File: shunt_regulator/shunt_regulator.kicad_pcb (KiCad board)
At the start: 2 copper layers, 87.5 x 94 mm, 58 parts, among them J1 Screw_Terminal_01x03, Q1 BC846B, Q2 BC846B, Q3 BC856B, Q4 30N06, U1 LM317_TO-252, U2 LM393

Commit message: Fixed a push-pull transistor that was the wrong way around
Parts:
- moved Q3 0.11 mm to (26.2, 18.5), turned to 90 degrees
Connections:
- Q3 pad 2: GND -> Net-(Q2-Pad2)
- Q3 pad 3: Net-(Q2-Pad2) -> GND
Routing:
- net Net-(Q3-Pad1): track 5.56 -> 7.08 mm
- net GND: track 84.0 -> 82.5 mm, vias 24 -> 25
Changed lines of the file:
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@@
   (net 6 "Net-(Q1-Pad1)")
   (net 7 "Net-(Q1-Pad2)")
-  (net 8 "Net-(Q2-Pad1)")
+  (net 8 "Net-(Q3-Pad1)")
   (net 9 "Net-(Q2-Pad2)")
   (net 10 "Net-(Q4-Pad1)")
@@
   )
   (footprint "Package_TO_SOT_SMD:SOT-23" (layer "F.Cu")
-    (at 26.162 18.431)
+    (at 26.162 18.542 90)
     (descr "SOT, 3 Pin (https://www.jedec.org/system/files/docs/to-236h.pdf variant AB), generated with kicad-footprint-generator ipc_gullwing_generator.py")
     (tags "SOT TO_SOT_SMD")
@@
     (property "Sheetname" "")
     (attr smd)
-    (fp_text reference "Q3" (at 3.838 1.069) (layer "F.SilkS")
-      (effects (font (size 1 1) (thickness 0.15)))
-    )
-    (fp_text value "BC856B" (at 0 2.4) (layer "F.Fab")
-      (effects (font (size 1 1) (thickness 0.15)))
-    )
-    (fp_text user "${REFERENCE}" (at 0 0) (layer "F.Fab")
+    (fp_text reference "Q3" (at 3.838 1.069 90) (layer "F.SilkS")
+      (effects (font (size 1 1) (thickness 0.15)))
+    )
+    (fp_text value "BC856B" (at 0 2.4 90) (layer "F.Fab")
+      (effects (font (size 1 1) (thickness 0.15)))
+    )
+    (fp_text user "${REFERENCE}" (at 0 0 90) (layer "F.Fab")
       (effects (font (size 0.32 0.32) (thickness 0.05)))
     )
@@
     (fp_line (start -0.65 -1.125) (end -0.325 -1.45) (layer "F.Fab") (width 0.1))
     (fp_line (start -0.65 1.45) (end -0.65 -1.125) (layer "F.Fab") (width 0.1))
-    (pad "1" smd roundrect (at -0.9375 -0.95) (size 1.475 0.6) (layers "F.Cu" "F.Paste" "F.Mask") (roundrect_rratio 0.25)
-      (net 8 "Net-(Q2-Pad1)") (pinfunction "B") (pintype "input"))
-    (pad "2" smd roundrect (at -0.9375 0.95) (size 1.475 0.6) (layers "F.Cu" "F.Paste" "F.Mask") (roundrect_rratio 0.25)
-      (net 2 "GND") (pinfunction "E") (pintype "passive"))
-    (pad "3" smd roundrect (at 0.9375 0) (size 1.475 0.6) (layers "F.Cu" "F.Paste" "F.Mask") (roundrect_rratio 0.25)
-      (net 9 "Net-(Q2-Pad2)") (pinfunction "C") (pintype "passive"))
+    (pad "1" smd roundrect (at -0.9375 -0.95 90) (size 1.475 0.6) (layers "F.Cu" "F.Paste" "F.Mask") (roundrect_rratio 0.25)
+      (net 8 "Net-(Q3-Pad1)") (pinfunction "B") (pintype "input"))
+    (pad "2" smd roundrect (at -0.9375 0.95 90) (size 1.475 0.6) (layers "F.Cu" "F.Paste" "F.Mask") (roundrect_rratio 0.25)
+      (net 9 "Net-(Q2-Pad2)") (pinfunction "E") (pintype "passive"))
+    (pad "3" smd roundrect (at 0.9375 0 90) (size 1.475 0.6) (layers "F.Cu" "F.Paste" "F.Mask") (roundrect_rratio 0.25)
+      (net 2 "GND") (pinfunction "C") (pintype "passive"))
     (model "${KICAD6_3DMODEL_DIR}/Package_TO_SOT_SMD.3dshapes/SOT-23.wrl"
       (offset (xyz 0 0 0))
@@
     (fp_line (start -0.65 -1.125) (end -0.325 -1.45) (layer "F.Fab") (width 0.1))
     (pad "1" smd roundrect (at -0.9375 -0.95 90) (size 1.475 0.6) (layers "F.Cu" "F.Paste" "F.Mask") (roundrect_rratio 0.25)
-      (net 8 "Net-(Q2-Pad1)") (pinfunction "B") (pintype "input"))
+      (net 8 "Net-(Q3-Pad1)") (pinfunction "B") (pintype "input"))
     (pad "2" smd roundrect (at -0.9375 0.95 90) (size 1.475 0.6) (layers "F.Cu" "F.Paste" "F.Mask") (roundrect_rratio 0.25)
       (net 9 "Net-(Q2-Pad2)") (pinfunction "E") (pintype "passive"))
@@
       (net 15 "Net-(R10-Pad1)") (pintype "passive"))
     (pad "2" smd roundrect (at 0.9125 0) (size 1.025 1.4) (layers "F.Cu" "F.Paste" "F.Mask") (roundrect_rratio 0.243902439)
-      (net 8 "Net-(Q2-Pad1)") (pintype "passive"))
+      (net 8 "Net-(Q3-Pad1)") (pintype "passive"))
     (model "${KICAD6_3DMODEL_DIR}/Resistor_SMD.3dshapes/R_0805_2012Metric.wrl"
       (offset (xyz 0 0 0))
@@
   (segment (start -21.474528 12.346528) (end -19.431 10.303) (width 1) (layer "B.Cu") (net 1))
   (segment (start 44.726 4.969) (end 44.218 4.461) (width 2) (layer "F.Cu") (net 2))
-  (segment (start 28.645 19.631) (end 28.702 19.574) (width 1) (layer "F.Cu") (net 2))
   (segment (start 46.99 4.461) (end 45.466 4.461) (width 2) (layer "F.Cu") (net 2))
-  (segment (start 25.2245 19.381) (end 25.4745 19.631) (width 1) (layer "F.Cu") (net 2))
   (segment (start 45.593 6.62) (end 46.47 6.62) (width 2) (layer "F.Cu") (net 2))
   (segment (start 48.768 8.652) (end 47.752 8.652) (width 2) (layer "F.Cu") (net 2))
@@
   (segment (start 48.768 8.62011) (end 48.768 8.652) (width 2) (layer "F.Cu") (net 2))
   (segment (start 43.978 8.652) (end 44.218 8.412) (width 2) (layer "F.Cu") (net 2))
+  (segment (start 25.2245 17.6045) (end 25.146 17.526) (width 1) (layer "F.Cu") (net 2))
   (segment (start 23.005 11.591) (end 22.987 11.573) (width 1) (layer "F.Cu") (net 2))
   (segment (start 46.228 8.652) (end 44.704 8.652) (width 2) (layer "F.Cu") (net 2))
+  (segment (start 27.0995 17.6045) (end 27.178 17.526) (width 1) (layer "F.Cu") (net 2))
   (segment (start -27.7105 18.558) (end -27.7105 20.0575) (width 1) (layer "F.Cu") (net 2))
+  (segment (start 26.162 17.6045) (end 27.0995 17.6045) (width 1) (layer "F.Cu") (net 2))
   (segment (start 41.656 8.652) (end 43.18 8.652) (width 2) (layer "F.Cu") (net 2))
   (segment (start 24.3355 11.591) (end 23.005 11.591) (width 1) (layer "F.Cu") (net 2))
@@
   (segment (start 3.1515 19.574) (end 2.447 19.574) (width 1) (layer "F.Cu") (net 2))
   (segment (start 2.447 19.574) (end 1.778 18.905) (width 1) (layer "F.Cu") (net 2))
-  (segment (start 27.051 19.631) (end 28.645 19.631) (width 1) (layer "F.Cu") (net 2))
   (segment (start 46.978 6.112) (end 46.978 5.846) (width 2) (layer "F.Cu") (net 2))
   (segment (start 47.752 8.652) (end 46.228 8.652) (width 2) (layer "F.Cu") (net 2))
@@
   (segment (start 46.978 6.83011) (end 48.768 8.62011) (width 2) (layer "F.Cu") (net 2))
   (segment (start 16.572 14.429) (end 16.51 14.367) (width 1) (layer "F.Cu") (net 2))
-  (segment (start 25.4745 19.631) (end 27.051 19.631) (width 1) (layer "F.Cu") (net 2))
   (segment (start 44.218 8.412) (end 44.218 6.62) (width 2) (layer "F.Cu") (net 2))
   (segment (start 2.9995 13.605) (end 1.143 13.605) (width 1) (layer "F.Cu") (net 2))
+  (segment (start 26.162 17.6045) (end 25.2245 17.6045) (width 1) (layer "F.Cu") (net 2))
   (segment (start 46.978 6.112) (end 46.978 6.83011) (width 2) (layer "F.Cu") (net 2))
   (segment (start 44.218 6.62) (end 45.593 6.62) (width 2) (layer "F.Cu") (net 2))
@@
   (via (at 1.778 18.905) (size 1) (drill 0.5) (layers "F.Cu" "B.Cu") (net 2))
   (via (at 41.656 8.652) (size 1) (drill 0.5) (layers "F.Cu" "B.Cu") (net 2))
-  (via (at 28.702 19.574) (size 1) (drill 0.5) (layers "F.Cu" "B.Cu") (net 2))
   (via (at 45.593 6.62) (size 1) (drill 0.5) (layers "F.Cu" "B.Cu") (net 2))
   (via (at 41.452 18) (size 1) (drill 0.5) (layers "F.Cu" "B.Cu") (net 2))
@@
   (via (at -27.686 20.082) (size 1) (drill 0.5) (layers "F.Cu" "B.Cu") (net 2))
   (via (at 44.5 18) (size 1) (drill 0.5) (layers "F.Cu" "B.Cu") (net 2))
+  (via (at 27.178 17.526) (size 1) (drill 0.5) (layers "F.Cu" "B.Cu") (net 2))
   (via (at 46.024 18) (size 1) (drill 0.5) (layers "F.Cu" "B.Cu") (net 2))
   (via (at 49.072 18) (size 1) (drill 0.5) (layers "F.Cu" "B.Cu") (net 2))
@@
   (via (at 42.976 18) (size 1) (drill 0.5) (layers "F.Cu" "B.Cu") (net 2))
   (via (at 45.466 4.461) (size 1) (drill 0.5) (layers "F.Cu" "B.Cu") (net 2))
+  (via (at 25.146 17.526) (size 1) (drill 0.5) (layers "F.Cu" "B.Cu") (net 2))
   (via (at 47.752 8.652) (size 1) (drill 0.5) (layers "F.Cu" "B.Cu") (net 2))
   (via (at 44.218 4.461) (size 1) (drill 0.5) (layers "F.Cu" "B.Cu") (net 2))
@@
   (segment (start 6.858 17.7725) (end 5.196 17.7725) (width 1) (layer "F.Cu") (net 7))
   (segment (start 4.9765 17.553) (end 4.887 17.4635) (width 1) (layer "F.Cu") (net 7))
-  (segment (start 22.78 19.193) (end 22.78 18.384) (width 1) (layer "F.Cu") (net 8))
-  (segment (start 23.683 17.481) (end 25.2245 17.481) (width 1) (layer "F.Cu") (net 8))
-  (segment (start 22.78 18.384) (end 23.683 17.481) (width 1) (layer "F.Cu") (net 8))
-  (segment (start 25.212 17.4685) (end 25.2245 17.481) (width 1) (layer "F.Cu") (net 8))
-  (segment (start 25.212 15.5585) (end 25.212 17.4685) (width 1) (layer "F.Cu") (net 8))
-  (segment (start 27.0995 18.431) (end 28.074 17.4565) (width 1) (layer "F.Cu") (net 9))
-  (segment (start 28.074 17.4565) (end 30.734 17.4565) (width 1) (layer "F.Cu") (net 9))
-  (segment (start 27.112 18.4185) (end 27.0995 18.431) (width 1) (layer "F.Cu") (net 9))
-  (segment (start 27.112 15.5585) (end 27.112 18.4185) (width 1) (layer "F.Cu") (net 9))
+  (segment (start 23.622 18.796) (end 24.019 19.193) (width 1) (layer "F.Cu") (net 8))
+  (segment (start 25.212 15.5585) (end 25.0815 15.5585) (width 1) (layer "F.Cu") (net 8))
+  (segment (start 25.212 19.4795) (end 24.3055 19.4795) (width 1) (layer "F.Cu") (net 8))
+  (segment (start 25.0815 15.5585) (end 23.622 17.018) (width 1) (layer "F.Cu") (net 8))
+  (segment (start 24.3055 19.4795) (end 24.019 19.193) (width 1) (layer "F.Cu") (net 8))
+  (segment (start 23.622 17.018) (end 23.622 18.796) (width 1) (layer "F.Cu") (net 8))
+  (segment (start 24.019 19.193) (end 22.78 19.193) (width 1) (layer "F.Cu") (net 8))
+  (segment (start 27.2425 15.5585) (end 28.702 17.018) (width 1) (layer "F.Cu") (net 9))
+  (segment (start 27.112 15.5585) (end 27.2425 15.5585) (width 1) (layer "F.Cu") (net 9))
+  (segment (start 28.702 17.8895) (end 27.112 19.4795) (width 1) (layer "F.Cu") (net 9))
+  (segment (start 28.702 17.018) (end 28.702 17.8895) (width 1) (layer "F.Cu") (net 9))
+  (segment (start 29.135 17.4565) (end 28.702 17.8895) (width 1) (layer "F.Cu") (net 9))
+  (segment (start 30.5 17.4565) (end 29.135 17.4565) (width 1) (layer "F.Cu") (net 9))
   (segment (start 32.319611 8.844389) (end 32.319611 9.945889) (width 1) (layer "F.Cu") (net 10))
   (segment (start 40.421003 4.08) (end 37.084 4.08) (width 1) (layer "F.Cu") (net 10))

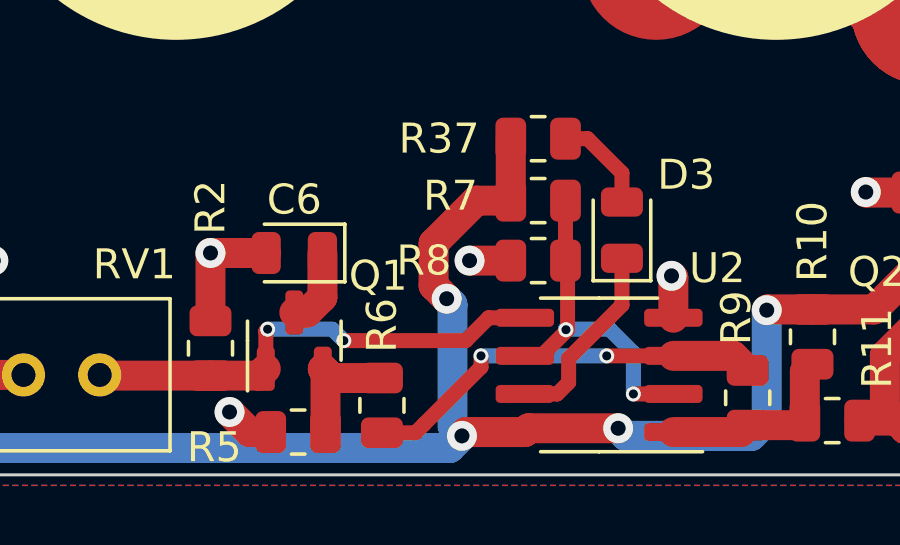
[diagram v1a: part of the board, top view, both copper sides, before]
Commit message: Flipped input of LED comperator
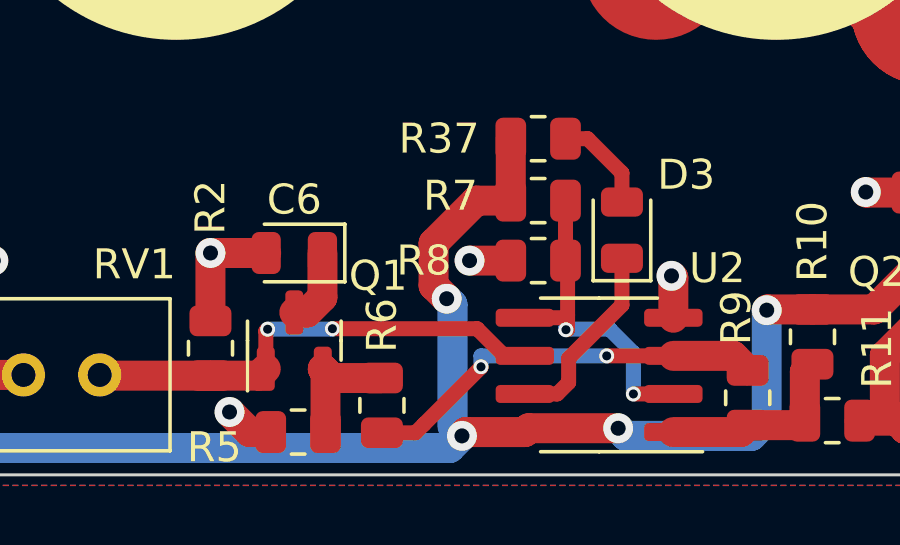
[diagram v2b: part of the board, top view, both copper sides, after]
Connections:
- Q1 pad 1: Net-(Q1-Pad1) -> Net-(U2-Pad6)
- R2 pad 2: Net-(Q1-Pad1) -> Net-(U2-Pad6)
- R7 pad 2: Net-(R7-Pad2) -> Net-(U2-Pad5)
- R8 pad 2: Net-(R7-Pad2) -> Net-(U2-Pad5)
- RV1 pad 3: Net-(Q1-Pad1) -> Net-(U2-Pad6)
- U2 pad 2: Net-(R7-Pad2) -> Net-(U2-Pad5)
- U2 pad 5: Net-(Q1-Pad1) -> Net-(U2-Pad5)
- U2 pad 6: Net-(R7-Pad2) -> Net-(U2-Pad6)
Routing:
- net Net-(U2-Pad6): track 0.00 -> 16.5 mm, vias 0 -> 2
- net Net-(Q1-Pad1): track 16.0 -> 0.00 mm, vias 2 -> 0
- net Net-(R7-Pad2): track 11.4 -> 0.00 mm, vias 2 -> 0
- net Net-(U2-Pad5): track 0.00 -> 11.1 mm, vias 0 -> 2

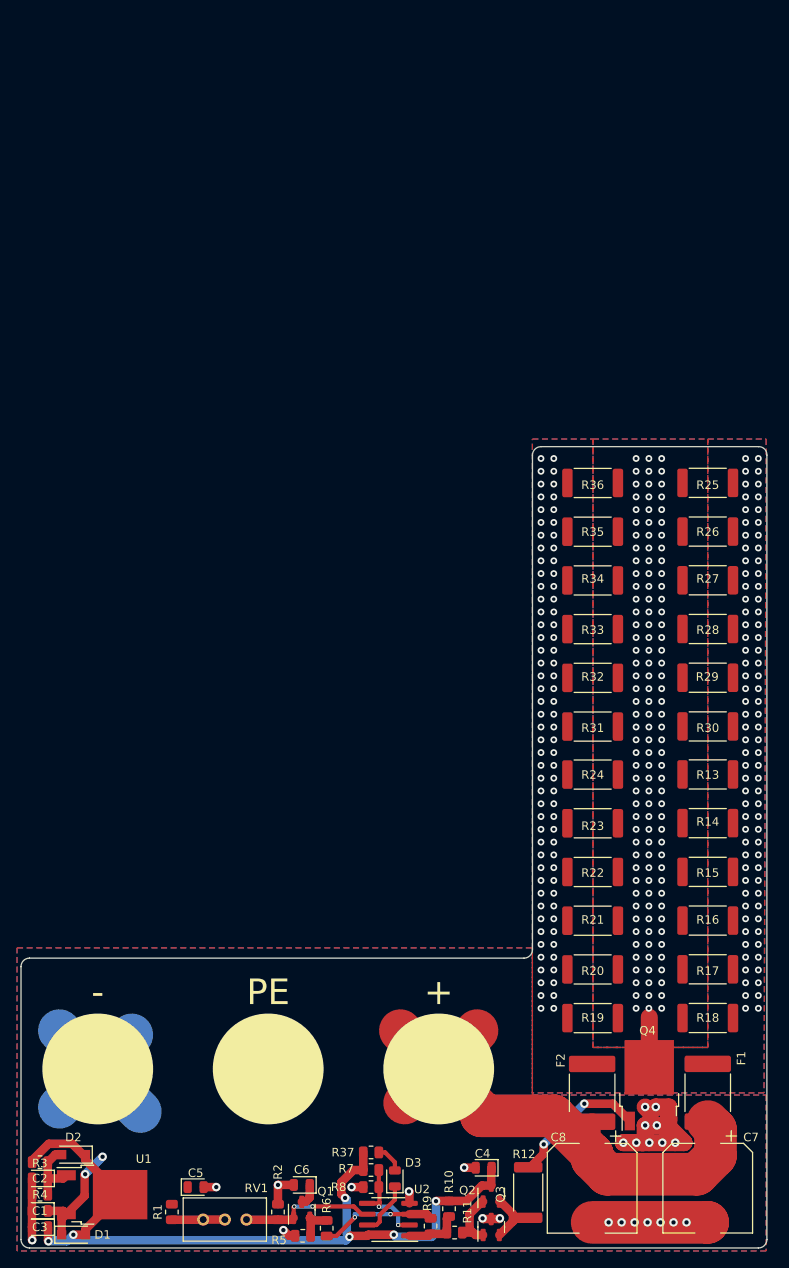
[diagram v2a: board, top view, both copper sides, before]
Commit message: Created more space for dissipation resistors, this way less heat is dunped into the fuses (increasing their rating)
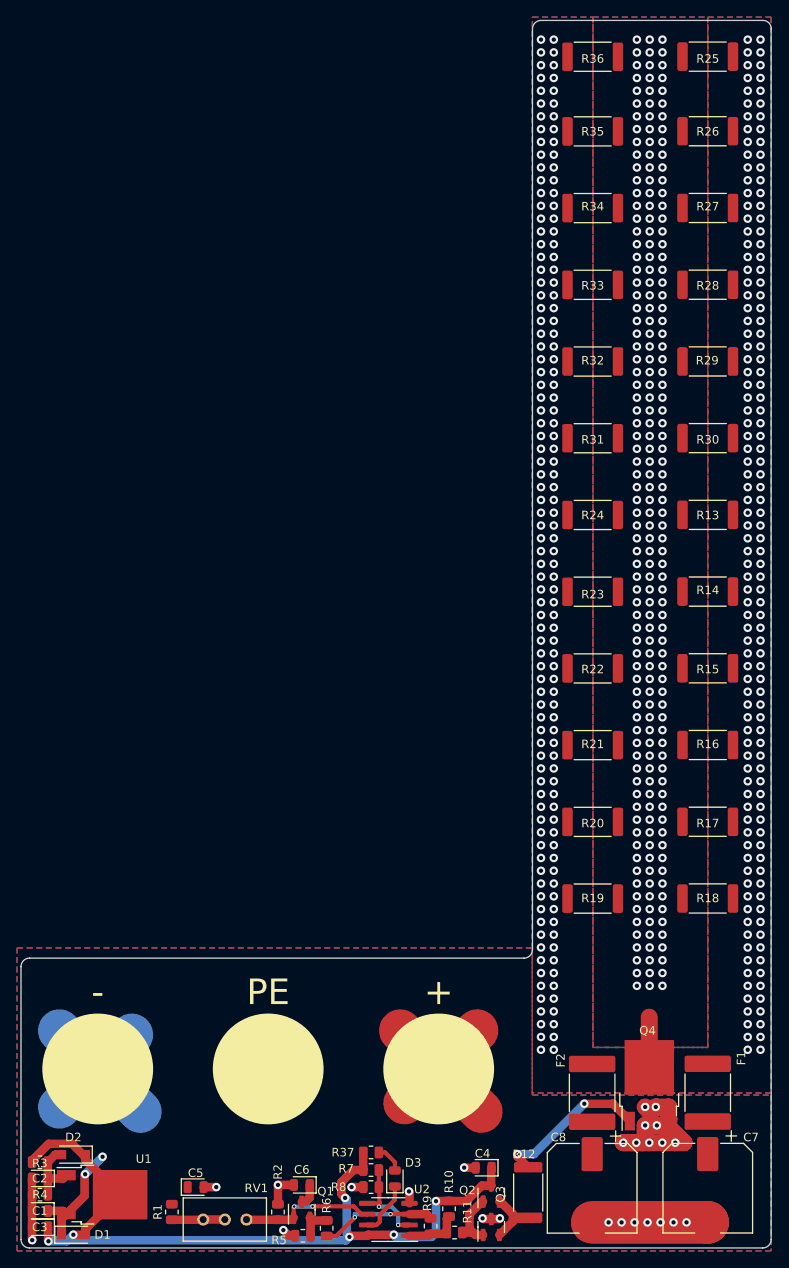
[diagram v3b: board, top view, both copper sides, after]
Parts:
- moved R25 50.0 mm to (51.6, -118.8)
- moved R36 50.0 mm to (38.1, -118.7)
- moved R26 47.0 mm to (51.6, -110.0)
- moved R35 47.0 mm to (38.1, -110.0)
- moved R34 43.7 mm to (38.1, -101.0)
- moved R27 43.7 mm to (51.6, -101.0)
- moved R33 40.4 mm to (38.1, -92.0)
- moved R28 40.4 mm to (51.6, -92.0)
- moved R32 37.1 mm to (38.1, -83.0)
- moved R29 37.1 mm to (51.6, -83.0)
- moved R31 33.8 mm to (38.1, -74.0)
- moved R30 33.8 mm to (51.6, -74.0)
- moved R24 30.5 mm to (38.1, -65.0)
- moved R13 30.5 mm to (51.6, -65.0)
- moved R14 27.2 mm to (51.6, -56.0)
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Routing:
- net +VDC: track 85.7 -> 41.6 mm
- net Net-(Q4-Pad1): track 16.3 -> 18.5 mm
- net Net-(Q4-Pad2): vias 132 -> 225
- net Net-(F2-Pad2): vias 88 -> 160
- net Net-(F1-Pad2): vias 88 -> 160
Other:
- board size 87.5 x 94 mm -> 88 x 144 mm
